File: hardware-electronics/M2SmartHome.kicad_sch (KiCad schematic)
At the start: 5 parts, among them J1 M.2-Key-M-edge-connector

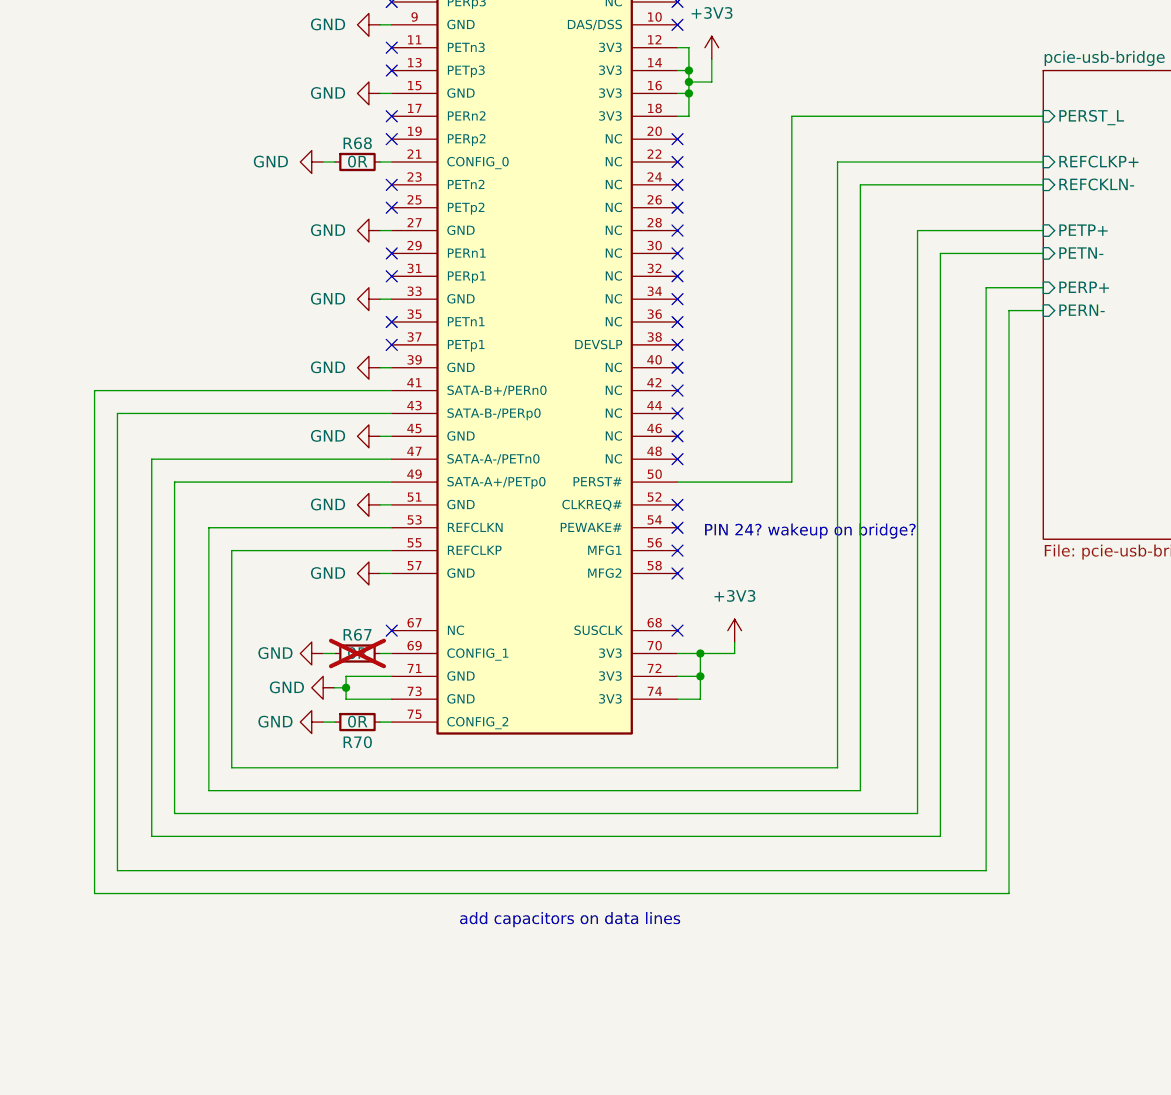
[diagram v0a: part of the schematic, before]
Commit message: SCH add series capacitors on PCIe lines
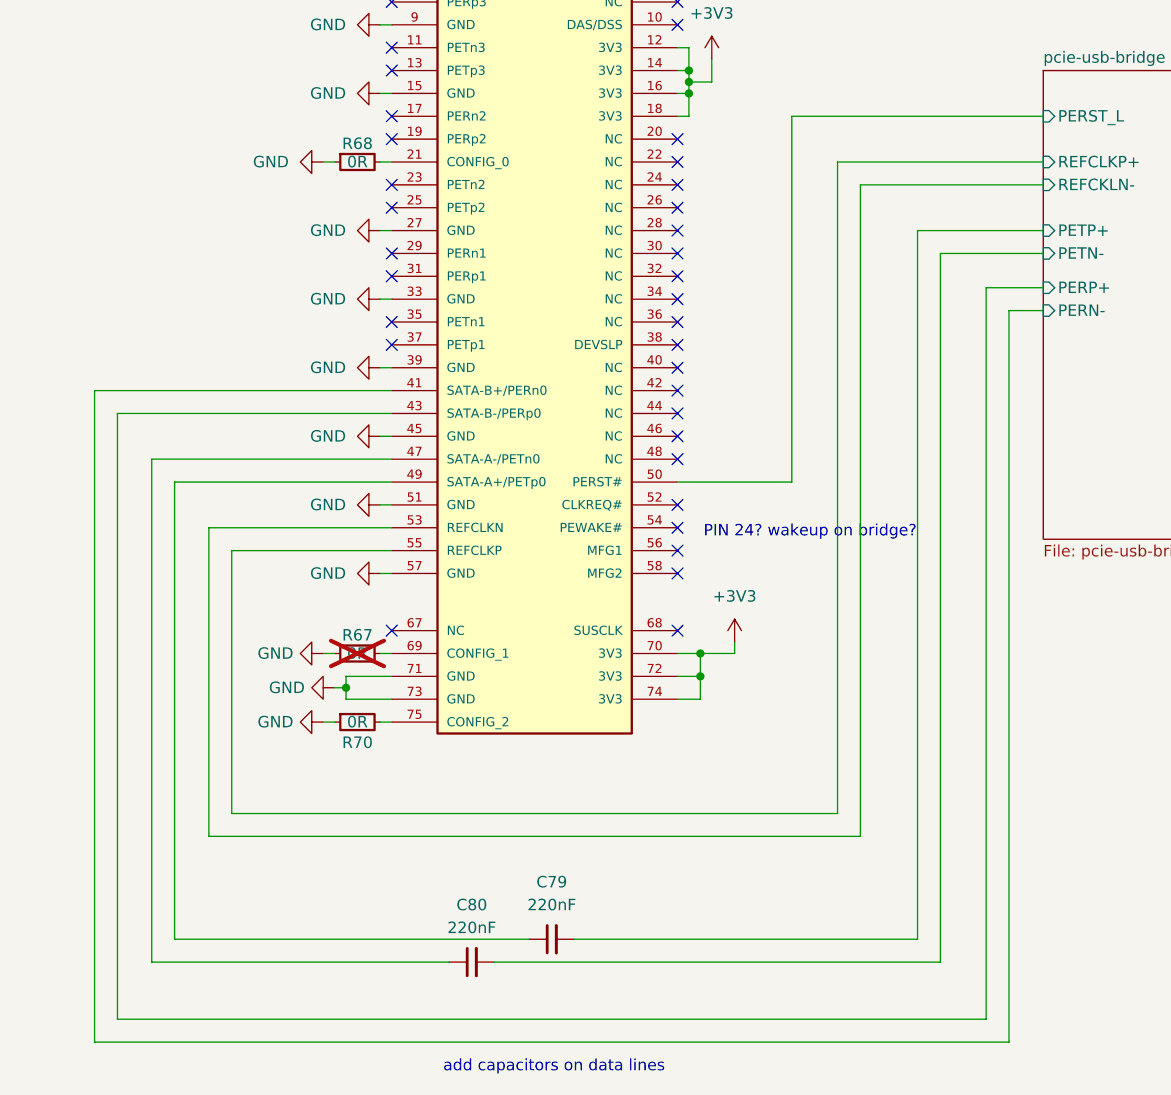
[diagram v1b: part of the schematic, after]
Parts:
- added C79, C80: C_220nF_0402, M2SmartHomeFootprints:C_0402, symbol M2SmartHomeSymbols:C_220nF_0402
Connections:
- net pcie-usb-bridge/PETN-: now also C80.2; no longer J1.47 (SATA-A-/PETn0)
- net pcie-usb-bridge/PETP+: now also C79.2; no longer J1.49 (SATA-A+/PETp0)
- new net: C80.1, J1.47 (SATA-A-/PETn0)
- new net: C79.1, J1.49 (SATA-A+/PETp0)

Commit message: SCH fill info box
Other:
- title: (none) -> M2SmartHome
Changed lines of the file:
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@@
 	(generator_version "8.0")
 	(paper "A3")
+	(title_block
+		(title "M2SmartHome")
+		(date "2024-10-11")
+		(rev "Rev 1.0.0")
+	)
 	(junction
 		(at 137.16 57.15)

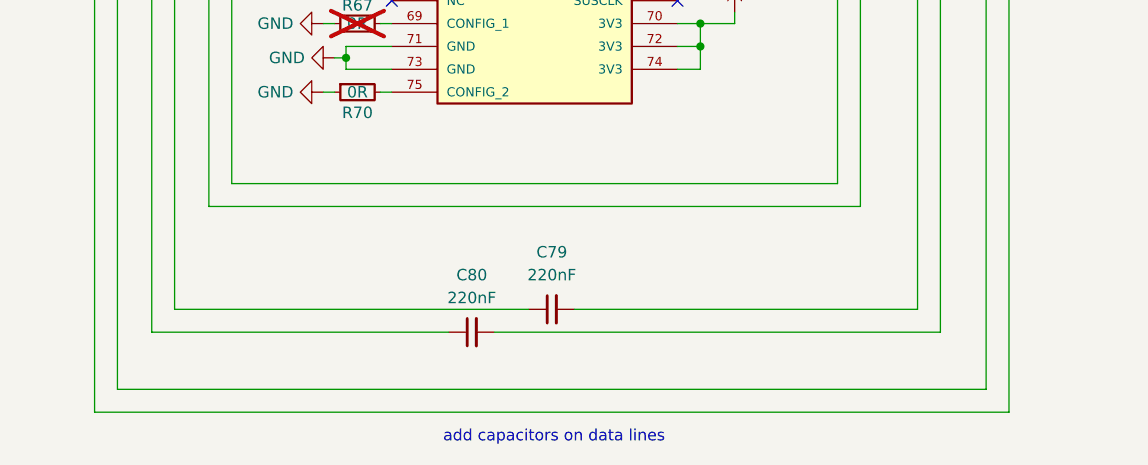
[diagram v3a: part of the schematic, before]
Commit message: [#15] Defined net class for PCIe
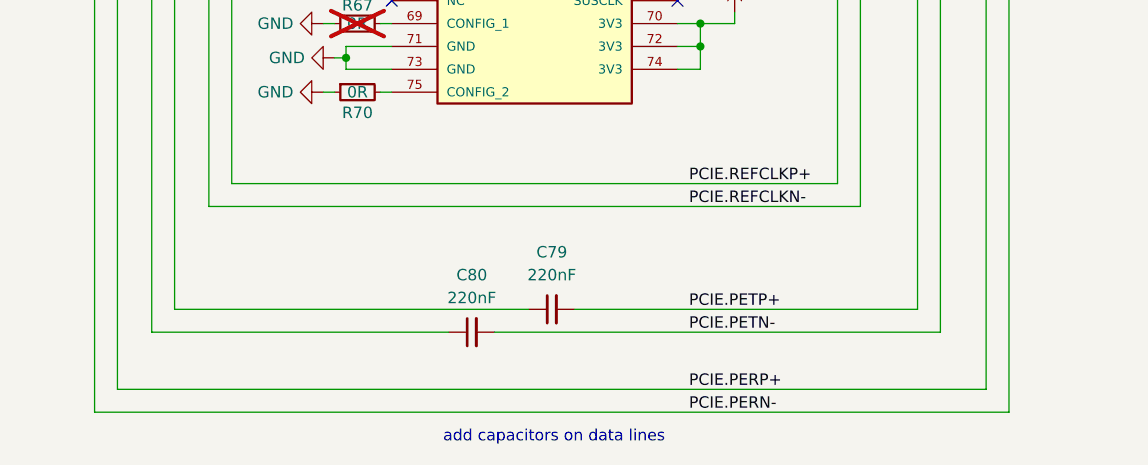
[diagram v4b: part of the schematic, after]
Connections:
- net pcie-usb-bridge/PERN- renamed PCIE.PERN-
- net pcie-usb-bridge/PERP+ renamed PCIE.PERP+
- net pcie-usb-bridge/PETN- renamed PCIE.PETN-
- net pcie-usb-bridge/PETP+ renamed PCIE.PETP+
- net pcie-usb-bridge/REFCKLN- renamed PCIE.REFCLKN-
- net pcie-usb-bridge/REFCLKP+ renamed PCIE.REFCLKP+
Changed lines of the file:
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@@
-	(wire
-		(pts
-			(xy 170.18 162.56) (xy 73.66 162.56)
-		)
-		(stroke
-			(width 0)
-			(type default)
-		)
-	)
 	(wire
 		(pts
@@
 	(wire
 		(pts
+			(xy 83.82 142.24) (xy 156.21 142.24)
+		)
+		(stroke
+			(width 0)
+			(type default)
+		)
+	)
+	(wire
+		(pts
 			(xy 232.41 87.63) (xy 270.51 87.63)
 		)
@@
 	(wire
 		(pts
+			(xy 73.66 162.56) (xy 170.18 162.56)
+		)
+		(stroke
+			(width 0)
+			(type default)
+		)
+	)
+	(wire
+		(pts
 			(xy 142.24 121.92) (xy 142.24 120.65)
 		)
@@
 		(pts
 			(xy 104.14 92.71) (xy 71.12 92.71)
-		)
-		(stroke
-			(width 0)
-			(type default)
-		)
-	)
-	(wire
-		(pts
-			(xy 156.21 142.24) (xy 83.82 142.24)
 		)
 		(stroke
@@
 		)
 	)
+	(label "PCIE.REFCLKP+"
+		(at 137.16 139.7 0)
+		(fields_autoplaced yes)
+		(effects
+			(font
+				(size 1.27 1.27)
+			)
+			(justify left bottom)
+		)
+	)
+	(label "PCIE.PETN-"
+		(at 137.16 156.21 0)
+		(fields_autoplaced yes)
+		(effects
+			(font
+				(size 1.27 1.27)
+			)
+			(justify left bottom)
+		)
+	)
+	(label "PCIE.PERN-"
+		(at 137.16 165.1 0)
+		(fields_autoplaced yes)
+		(effects
+			(font
+				(size 1.27 1.27)
+			)
+			(justify left bottom)
+		)
+	)
+	(label "PCIE.PERP+"
+		(at 137.16 162.56 0)
+		(fields_autoplaced yes)
+		(effects
+			(font
+				(size 1.27 1.27)
+			)
+			(justify left bottom)
+		)
+	)
+	(label "PCIE.PETP+"
+		(at 137.16 153.67 0)
+		(fields_autoplaced yes)
+		(effects
+			(font
+				(size 1.27 1.27)
+			)
+			(justify left bottom)
+		)
+	)
+	(label "PCIE.REFCLKN-"
+		(at 137.16 142.24 0)
+		(fields_autoplaced yes)
+		(effects
+			(font
+				(size 1.27 1.27)
+			)
+			(justify left bottom)
+		)
+	)

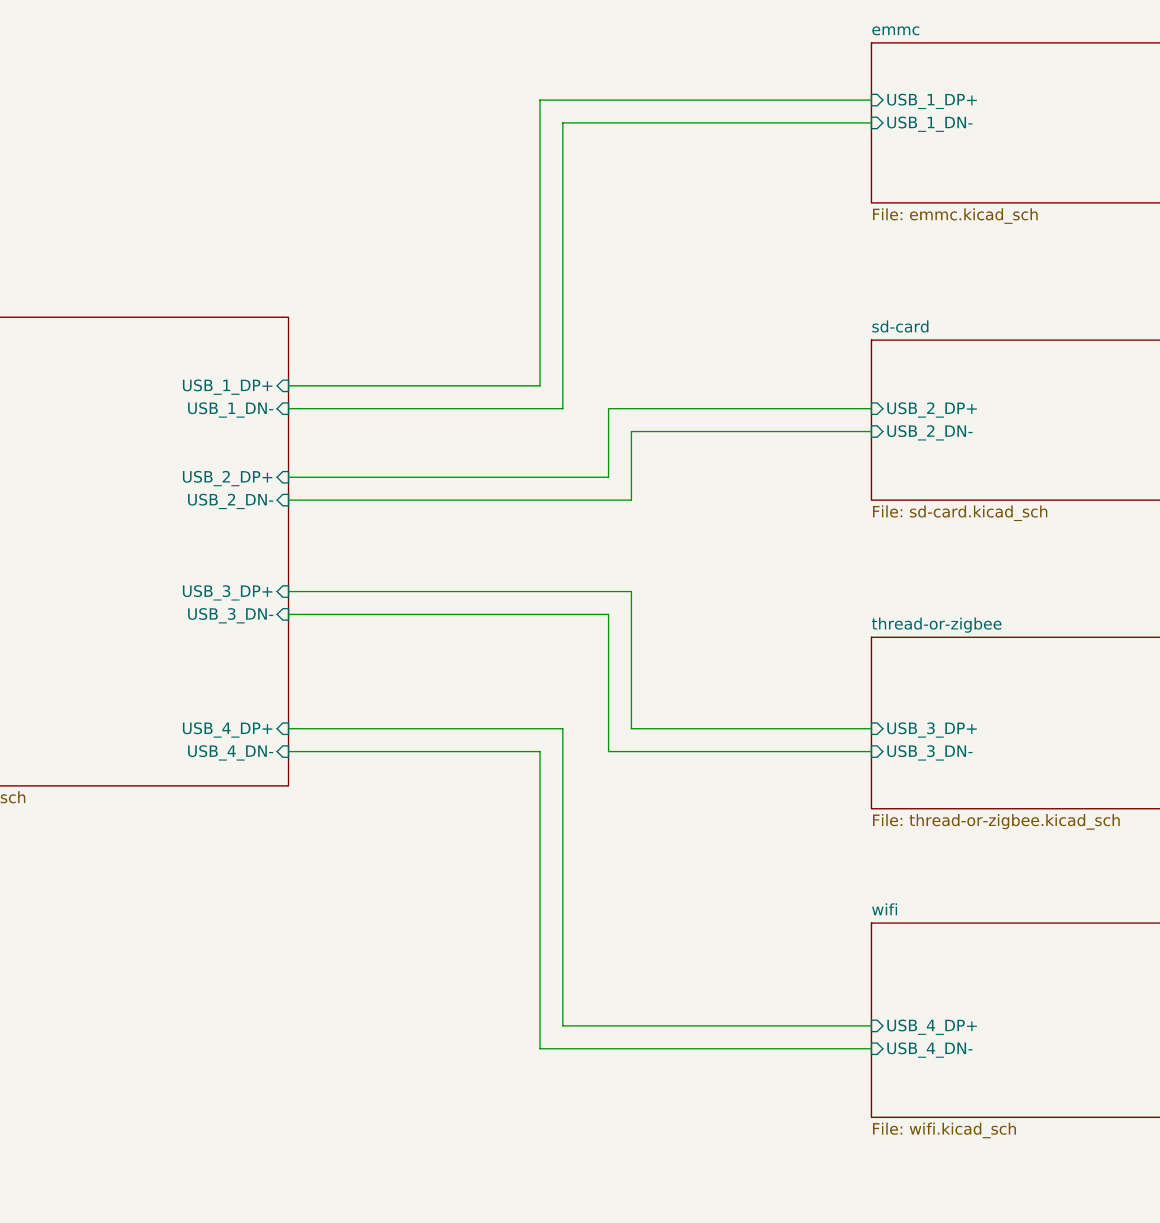
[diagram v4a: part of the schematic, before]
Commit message: [#17] Rename USB signals
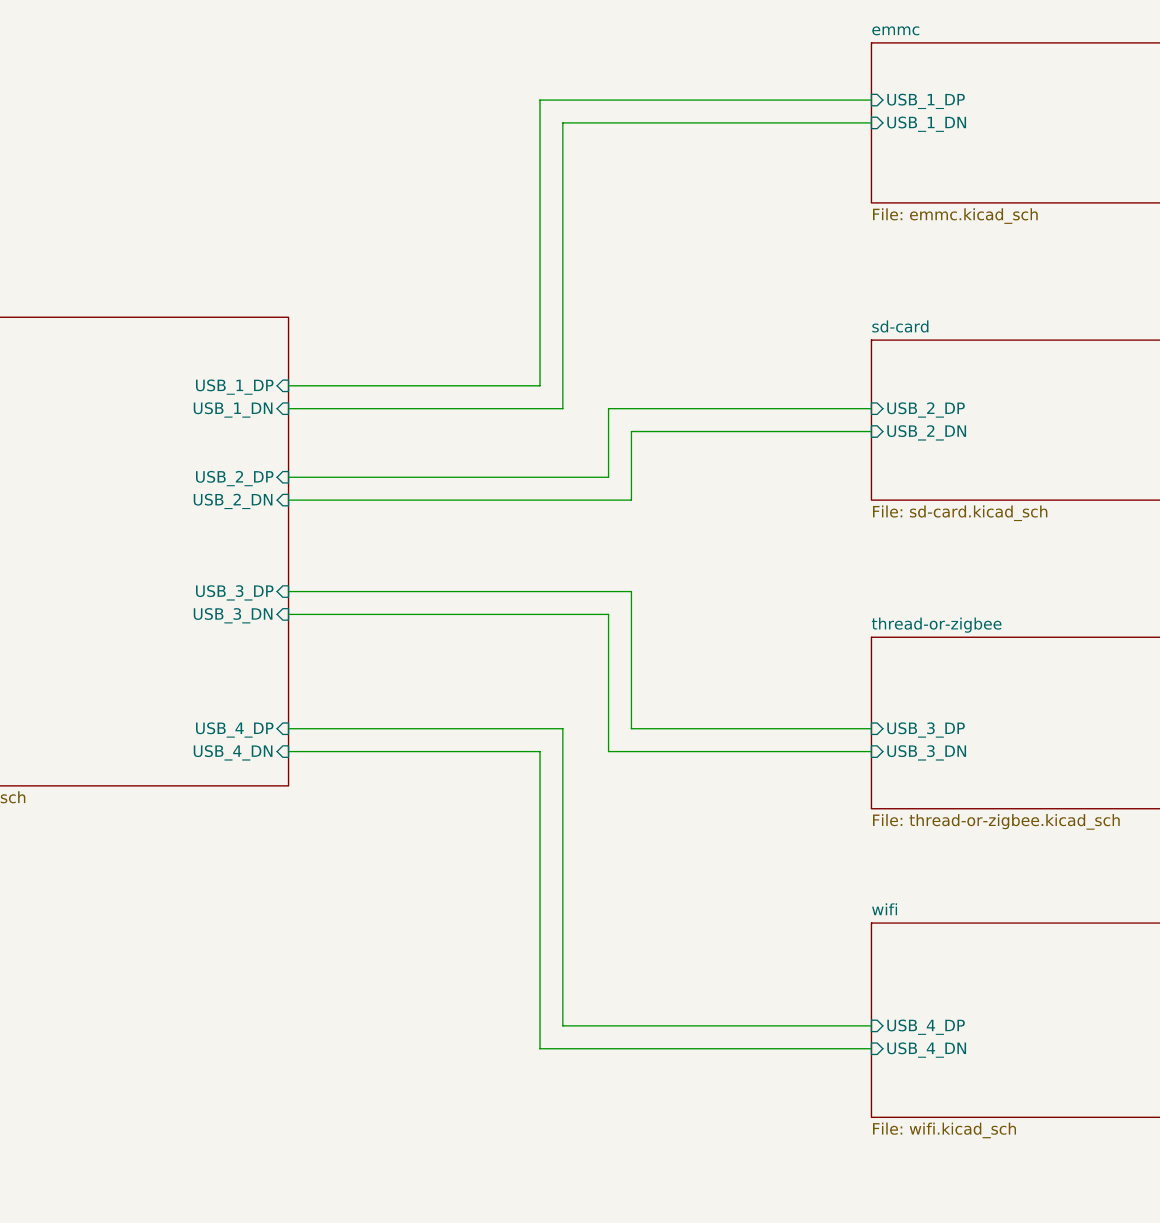
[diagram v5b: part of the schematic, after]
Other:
- sheet emmc ports: added USB_1_DN, USB_1_DP; removed USB_1_DN-, USB_1_DP+
- sheet pcie-usb-bridge ports: added USB_1_DN, USB_1_DP, USB_2_DN, USB_2_DP, USB_3_DN, USB_3_DP, USB_4_DN, USB_4_DP; removed USB_1_DN-, USB_1_DP+, USB_2_DN-, USB_2_DP+, USB_3_DN-, USB_3_DP+, USB_4_DN-, USB_4_DP+
- sheet sd-card ports: added USB_2_DN, USB_2_DP; removed USB_2_DN-, USB_2_DP+
- sheet thread-or-zigbee ports: added USB_3_DN, USB_3_DP; removed USB_3_DN-, USB_3_DP+
- sheet wifi ports: added USB_4_DN, USB_4_DP; removed USB_4_DN-, USB_4_DP+
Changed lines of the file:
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@@
 			)
 		)
-		(pin "USB_2_DN-" input
+		(pin "USB_2_DN" input
 			(at 297.18 69.85 180)
 			(effects
@@
 			)
 		)
-		(pin "USB_2_DP+" input
+		(pin "USB_2_DP" input
 			(at 297.18 67.31 180)
 			(effects
@@
 			)
 		)
-		(pin "USB_4_DN-" input
+		(pin "USB_4_DN" input
 			(at 297.18 138.43 180)
 			(effects
@@
 			)
 		)
-		(pin "USB_4_DP+" input
+		(pin "USB_4_DP" input
 			(at 297.18 135.89 180)
 			(effects
@@
 			)
 		)
-		(pin "USB_3_DN-" input
+		(pin "USB_3_DN" input
 			(at 297.18 105.41 180)
 			(effects
@@
 			)
 		)
-		(pin "USB_3_DP+" input
+		(pin "USB_3_DP" input
 			(at 297.18 102.87 180)
 			(effects
@@
 			)
 		)
-		(pin "USB_3_DN-" input
+		(pin "USB_3_DN" input
 			(at 232.41 90.17 0)
 			(effects
@@
 			)
 		)
-		(pin "USB_3_DP+" input
+		(pin "USB_3_DP" input
 			(at 232.41 87.63 0)
 			(effects
@@
 			)
 		)
-		(pin "USB_4_DP+" input
+		(pin "USB_4_DP" input
 			(at 232.41 102.87 0)
 			(effects
@@
 			)
 		)
-		(pin "USB_2_DN-" input
+		(pin "USB_2_DN" input
 			(at 232.41 77.47 0)
 			(effects
@@
 			)
 		)
-		(pin "USB_1_DN-" input
+		(pin "USB_1_DN" input
 			(at 232.41 67.31 0)
 			(effects
@@
 			)
 		)
-		(pin "USB_2_DP+" input
+		(pin "USB_2_DP" input
 			(at 232.41 74.93 0)
 			(effects
@@
 			)
 		)
-		(pin "USB_1_DP+" input
+		(pin "USB_1_DP" input
 			(at 232.41 64.77 0)
 			(effects
@@
 			)
 		)
-		(pin "USB_4_DN-" input
+		(pin "USB_4_DN" input
 			(at 232.41 105.41 0)
 			(effects
@@
 			)
 		)
-		(pin "USB_1_DP+" input
+		(pin "USB_1_DP" input
 			(at 297.18 33.02 180)
 			(effects
@@
 			)
 		)
-		(pin "USB_1_DN-" input
+		(pin "USB_1_DN" input
 			(at 297.18 35.56 180)
 			(effects

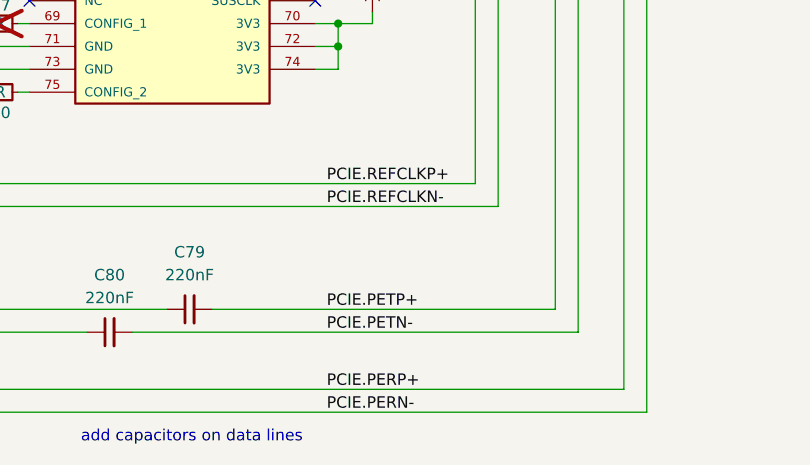
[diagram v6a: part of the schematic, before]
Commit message: [#17] PCIe renamed HS signals
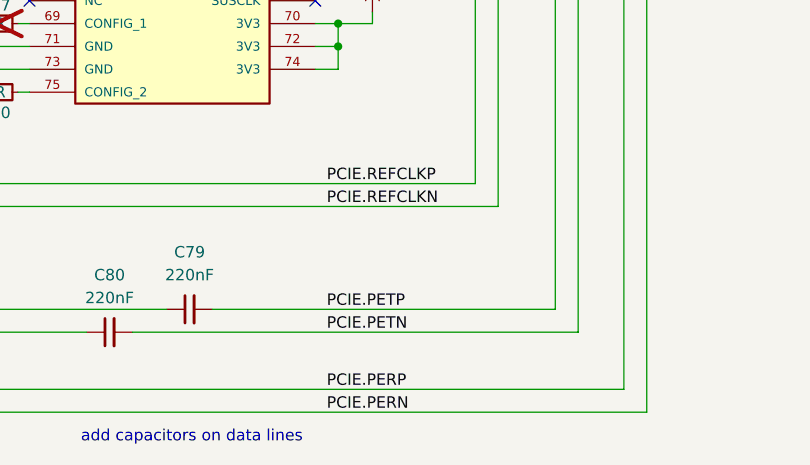
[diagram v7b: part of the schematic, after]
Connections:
- net PCIE.PERN- renamed PCIE.PERN
- net PCIE.PERP+ renamed PCIE.PERP
- net PCIE.PETN- renamed PCIE.PETN
- net PCIE.PETP+ renamed PCIE.PETP
- net PCIE.REFCLKN- renamed PCIE.REFCLKN
- net PCIE.REFCLKP+ renamed PCIE.REFCLKP
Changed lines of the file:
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@@
 		)
 	)
-	(label "PCIE.REFCLKP+"
+	(label "PCIE.REFCLKP"
 		(at 137.16 139.7 0)
 		(fields_autoplaced yes)
@@
 		)
 	)
-	(label "PCIE.PETN-"
+	(label "PCIE.PETN"
 		(at 137.16 156.21 0)
 		(fields_autoplaced yes)
@@
 		)
 	)
-	(label "PCIE.PERN-"
+	(label "PCIE.PERN"
 		(at 137.16 165.1 0)
 		(fields_autoplaced yes)
@@
 		)
 	)
-	(label "PCIE.PERP+"
+	(label "PCIE.PERP"
 		(at 137.16 162.56 0)
 		(fields_autoplaced yes)
@@
 		)
 	)
-	(label "PCIE.PETP+"
+	(label "PCIE.PETP"
 		(at 137.16 153.67 0)
 		(fields_autoplaced yes)
@@
 		)
 	)
-	(label "PCIE.REFCLKN-"
+	(label "PCIE.REFCLKN"
 		(at 137.16 142.24 0)
 		(fields_autoplaced yes)

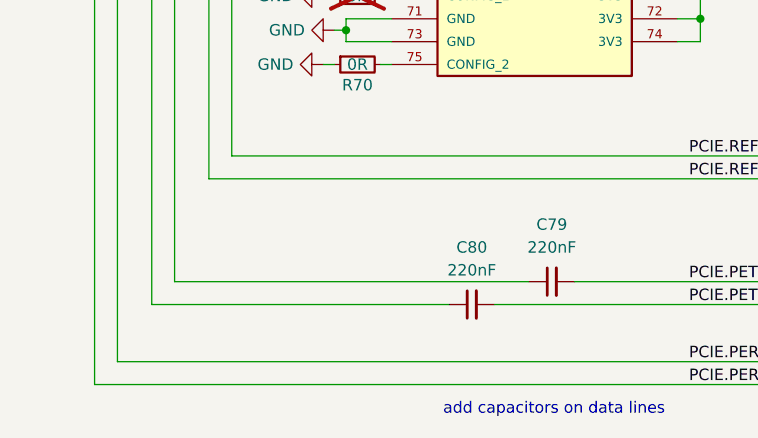
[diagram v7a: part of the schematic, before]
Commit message: [#17] PCIe WIP routing plan
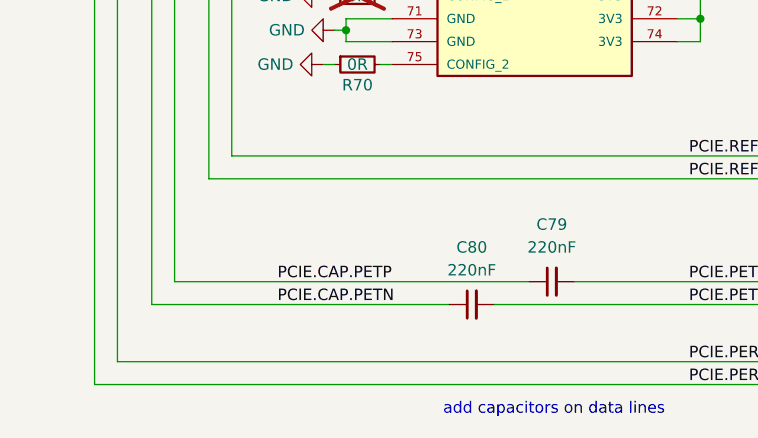
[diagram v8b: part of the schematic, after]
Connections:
- net PCIE.CAP.PETN: now reaches C80.1, J1.47 (SATA-A-/PETn0)
- net PCIE.CAP.PETP: now reaches C79.1, J1.49 (SATA-A+/PETp0)
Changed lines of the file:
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@@
+		)
+	)
+	(label "PCIE.CAP.PETN"
+		(at 91.44 156.21 0)
+		(fields_autoplaced yes)
+		(effects
+			(font
+				(size 1.27 1.27)
+			)
+			(justify left bottom)
 		)
 	)
@@
 		(fields_autoplaced yes)
 		(effects
+			(font
+				(size 1.27 1.27)
+			)
+			(justify left bottom)
+		)
+	)
+	(label "PCIE.CAP.PETP"
+		(at 91.44 153.67 0)
+		(fields_autoplaced yes)
+		(effects
